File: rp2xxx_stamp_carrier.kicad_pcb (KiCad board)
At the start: 4 copper layers, 101.6 x 53.3 mm, 259 parts, among them J1 Conn_Stemma_QT, J10 Conn_01x10, J11 microSD, J12 Conn_01x08, J13 Conn_SPI, J14 Conn_01x08, J15 Conn_01x08, J16 Conn_01x08, J17 USB_C_Receptacle_USB2.0, J18 USB_A, J2 Conn_Pi_SWD, J3 Conn_Pi_UART, J4 Conn_Batt, J5 Barrel_Jack, J6 DVI-D_Mini, J8 Conn_PMOD, J9 Conn_01x08, Q1 DMG3415U-7, SW1 BTN_RESET, SW2 BTN_BOOTSEL, SW3 SW_USB, SW4 BTN_USR1, SW5 BTN_USR2, U1 XL1509-5.0, U2 MSUSB30, U3 RP2350_Stamp_XL

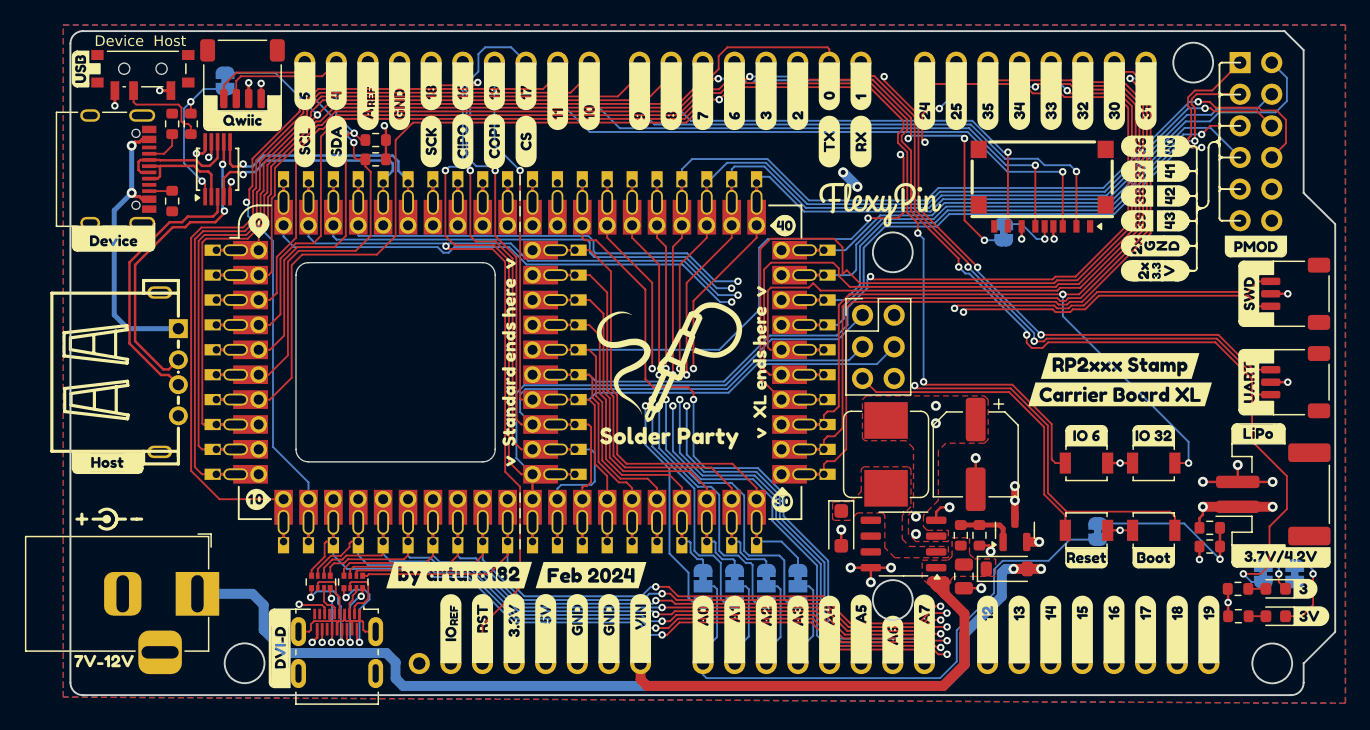
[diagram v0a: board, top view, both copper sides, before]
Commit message: Rev 2
Fixed HDMI connector
Swapped RST and BOOTSEL buttons to match Stamp
Added BAT_STAT to Stamp
Changed 2x silk back to single line
Adjusted Name silkscreen
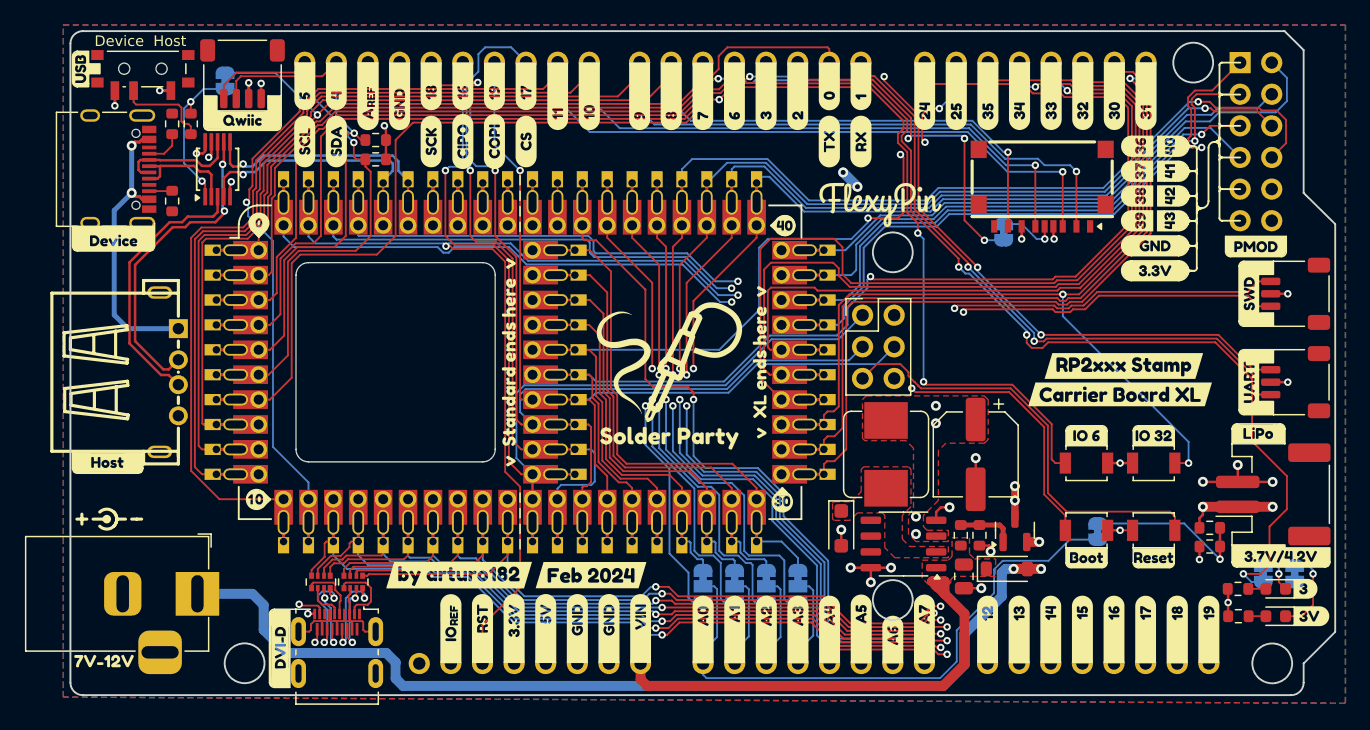
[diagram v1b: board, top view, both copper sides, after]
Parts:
- removed kibuzzard-65DBD93A (x2): G***, kibuzzard-65DBD93A
- removed kibuzzard-65DBD94E (x2): G***, kibuzzard-65DBD94E
- removed kibuzzard-65DBD952 (x2): G***, kibuzzard-65DBD952
- removed kibuzzard-65DBDA2E (x4): G***, kibuzzard-65DBDA2E
- removed kibuzzard-65DBDB16 (x2): G***, kibuzzard-65DBDB16
- removed kibuzzard-65DBDB2C (x2): G***, kibuzzard-65DBDB2C
- added kibuzzard-66063958: G***, kibuzzard-66063958, B.Cu at (195.4, 87.8)
- added kibuzzard-66063979: G***, kibuzzard-66063979, B.Cu at (195.4, 89.8)
- added kibuzzard-660639E8: G***, kibuzzard-660639E8, F.Cu at (195.7, 89.8)
- added kibuzzard-660639F3: G***, kibuzzard-660639F3, F.Cu at (195.7, 87.8)
- U3: value RP2350_Stamp_XL -> rp2xxx_Stamp_XL; footprint rp2350_stamp_carrier:RP2xx_Stamp_FlexyPin -> rp2xxx_stamp_carrier:RP2xx_Stamp_FlexyPin
- moved SW1 5.40 mm to (195.6, 110.6), turned to 0 degrees
- moved SW2 5.40 mm to (190.2, 110.6), turned to 180 degrees
- moved kibuzzard-65DBAE3B 5.40 mm to (195.6, 112.8)
- moved kibuzzard-65DBAE3E 5.40 mm to (190.2, 112.8)
- moved kibuzzard-65DBBE17 1.10 mm to (179.4, 101.3)
- moved kibuzzard-65DBBE25 0.80 mm to (181.7, 101.0)
- moved kibuzzard-65DBBE65 0.75 mm to (184.0, 100.6)
- moved kibuzzard-65DBBF1E 0.72 mm to (186.4, 100.2)
- moved kibuzzard-65DBBE17 0.30 mm to (193.2, 97.4)
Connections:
- J6 pad 1: GND -> unconnected-(J6-HPD/HEAC--Pad1)
- J6 pad 11: Net-(J6-CK+) -> Net-(J6-D0-)
- J6 pad 12: Net-(J6-CK-) -> Net-(J6-CK+)
- J6 pad 14: unconnected-(J6-CEC-Pad14) -> Net-(J6-CK-)
- J6 pad 15: /GPIO5 -> unconnected-(J6-CEC-Pad15)
- J6 pad 16: /GPIO4 -> GND
- J6 pad 17: unconnected-(J6-UTILITY/HEAC+-Pad17) -> /GPIO5
- J6 pad 18: +5V -> /GPIO4
- J6 pad 19: unconnected-(J6-HPD/HEAC--Pad19) -> +5V
- J6 pad 2: Net-(J6-D2+) -> unconnected-(J6-UTILITY/HEAC+-Pad2)
- J6 pad 3: Net-(J6-D2-) -> Net-(J6-D2+)
- J6 pad 5: Net-(J6-D1+) -> Net-(J6-D2-)
- J6 pad 6: Net-(J6-D1-) -> Net-(J6-D1+)
- J6 pad 8: Net-(J6-D0+) -> Net-(J6-D1-)
- J6 pad 9: Net-(J6-D0-) -> Net-(J6-D0+)
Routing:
- net /~{RESET}: track 120.8 -> 130.7 mm
- net /BOOTSEL: track 89.7 -> 81.2 mm
- net Net-(J6-D1+): track 2.35 -> 6.08 mm, vias 0 -> 2
- net Net-(J6-D0+): track 8.29 -> 4.91 mm, vias 2 -> 0
- net Net-(J6-CK+): track 2.70 -> 5.77 mm, vias 0 -> 2
- net Net-(J6-D2-): track 5.07 -> 2.16 mm
- net Net-(J6-D2+): track 8.47 -> 5.89 mm, vias 2 -> 0
- net Net-(J6-CK-): track 5.55 -> 8.06 mm
- net +5V: track 149.1 -> 151.1 mm
- net Net-(J6-D1-): track 6.05 -> 7.72 mm
- net unconnected-(U3A-BAT_STAT-Pad59): track 0.00 -> 1.55 mm
- net Net-(J6-D0-): track 4.45 -> 3.09 mm
- net GND: track 46.6 -> 45.9 mm

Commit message: Rev 3
- USB Switch jumper open by default
- Power USB Host from 5V not VBUS
- Fix SPI pin silkscreen
- Add test points for USB D+/D-
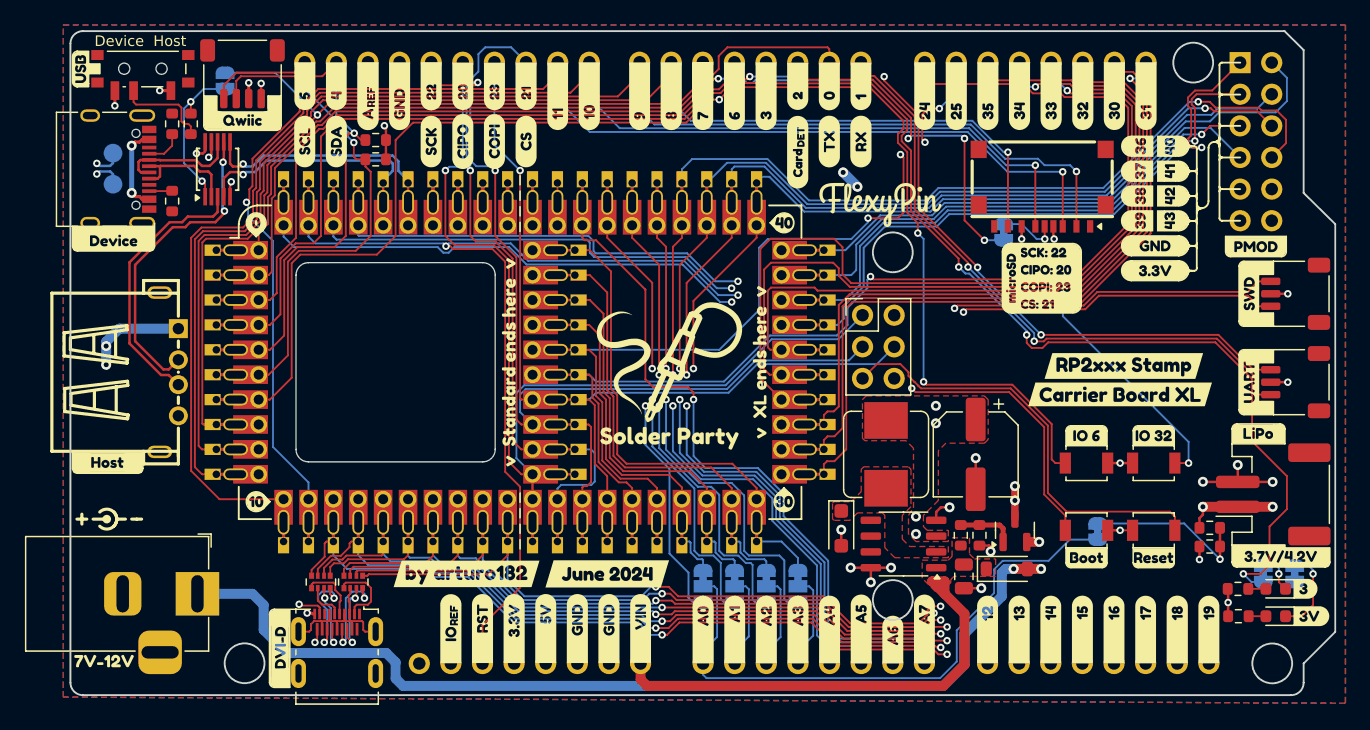
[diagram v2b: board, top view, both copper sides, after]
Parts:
- removed ? (x2): , buzzardLabel
- removed kibuzzard-653BCEA0: G***, kibuzzard-653BCEA0
- removed kibuzzard-653BD19C: G***, kibuzzard-653BD19C
- removed kibuzzard-65DA1421: G***, kibuzzard-65DA1421
- removed kibuzzard-65DA43F2: G***, kibuzzard-65DA43F2
- removed kibuzzard-65DA43F6: G***, kibuzzard-65DA43F6
- removed kibuzzard-65DA43F9: G***, kibuzzard-65DA43F9
- removed kibuzzard-65DA43FD: G***, kibuzzard-65DA43FD
- removed kibuzzard-65DB92FF: G***, kibuzzard-65DB92FF
- removed kibuzzard-65DB9306: G***, kibuzzard-65DB9306
- removed kibuzzard-65DB930D: G***, kibuzzard-65DB930D
- removed kibuzzard-65DB9314: G***, kibuzzard-65DB9314
- removed kibuzzard-65DBBF1E (x2): G***, kibuzzard-65DBBF1E
- added TP1: TP_USB_D+, TestPoint:TestPoint_Pad_D1.5mm, B.Cu at (112.0, 82.8)
- added TP2: TP_USB_D-, TestPoint:TestPoint_Pad_D1.5mm, B.Cu at (112.0, 80.3)
- added kibuzzard-65DA4391: G***, kibuzzard-65DA4391, F.Cu at (167.0, 77.8)
- added kibuzzard-65DA4391: G***, kibuzzard-65DA4391, F.Cu at (167.0, 82.7)
- added kibuzzard-668C75B1: G***, kibuzzard-668C75B1, F.Cu at (137.6, 74.9)
- added kibuzzard-668C75C6: G***, kibuzzard-668C75C6, F.Cu at (140.1, 74.9)
- added kibuzzard-668C75DA: G***, kibuzzard-668C75DA, F.Cu at (142.6, 74.9)
- added kibuzzard-668C7671: G***, kibuzzard-668C7671, F.Cu at (145.2, 74.9)
- added kibuzzard-668C76A7: G***, kibuzzard-668C76A7, B.Cu at (145.2, 75.0)
- added kibuzzard-668C7736: G***, kibuzzard-668C7736, B.Cu at (142.6, 75.0)
- added kibuzzard-668C7740: G***, kibuzzard-668C7740, B.Cu at (140.1, 75.0)
- added kibuzzard-668C7764: G***, kibuzzard-668C7764, B.Cu at (137.6, 74.9)
- added kibuzzard-668C8744: G***, kibuzzard-668C8744, F.Cu at (167.0, 74.9)
- added kibuzzard-668C88D6: G***, kibuzzard-668C88D6, F.Cu at (167.2, 79.0)
- added kibuzzard-668C88F2: G***, kibuzzard-668C88F2, F.Cu at (167.0, 81.1)
- added kibuzzard-668C89D9: G***, kibuzzard-668C89D9, F.Cu at (159.4, 74.9)
- added kibuzzard-668C9122: G***, kibuzzard-668C9122, F.Cu at (184.1, 90.3)
- added kibuzzard-668C9182: G***, kibuzzard-668C9182, F.Cu at (186.9, 90.3)
- added kibuzzard-668C9635: G***, kibuzzard-668C9635, B.Cu at (112.0, 78.2)
- added kibuzzard-668C97F2: G***, kibuzzard-668C97F2, B.Cu at (112.0, 84.9)
- added kibuzzard-6695ACF2: G***, kibuzzard-6695ACF2, F.Cu at (123.5, 108.3)
- added kibuzzard-6695AD18: G***, kibuzzard-6695AD18, F.Cu at (123.5, 85.9)
- added kibuzzard-6695BF60: G***, kibuzzard-6695BF60, F.Cu at (165.9, 108.3)
- added kibuzzard-6695BFEA: G***, kibuzzard-6695BFEA, F.Cu at (165.9, 85.9)
- added kibuzzard-6695CF81: G***, kibuzzard-6695CF81, F.Cu at (151.7, 114.1)
- added kibuzzard-6695CF95: G***, kibuzzard-6695CF95, B.Cu at (186.4, 100.2)
- J6: value DVI-D_Mini -> DVI-D_Micro
- JP4: footprint Jumper:SolderJumper-2_P1.3mm_Bridged_RoundedPad1.0x1.5mm -> Jumper:SolderJumper-2_P1.3mm_Open_RoundedPad1.0x1.5mm
- moved kibuzzard-65DBBE65 0.61 mm to (140.4, 114.1)
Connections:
- J18 pad 1: VBUS -> +5V
- U3 pad 59: unconnected-(U3A-BAT_STAT-Pad59) -> /BAT_STAT
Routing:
- net +5V: track 151.1 -> 188.4 mm, vias 8 -> 10
- net /USB_D+: track 19.1 -> 33.6 mm, vias 1 -> 2
- net /USB_D-: track 19.5 -> 33.9 mm, vias 1 -> 2
- net VBUS: track 118.7 -> 113.0 mm
- net unconnected-(U3A-BAT_STAT-Pad59): track 1.55 -> 0.00 mm
- net /BAT_STAT: track 0.00 -> 1.55 mm

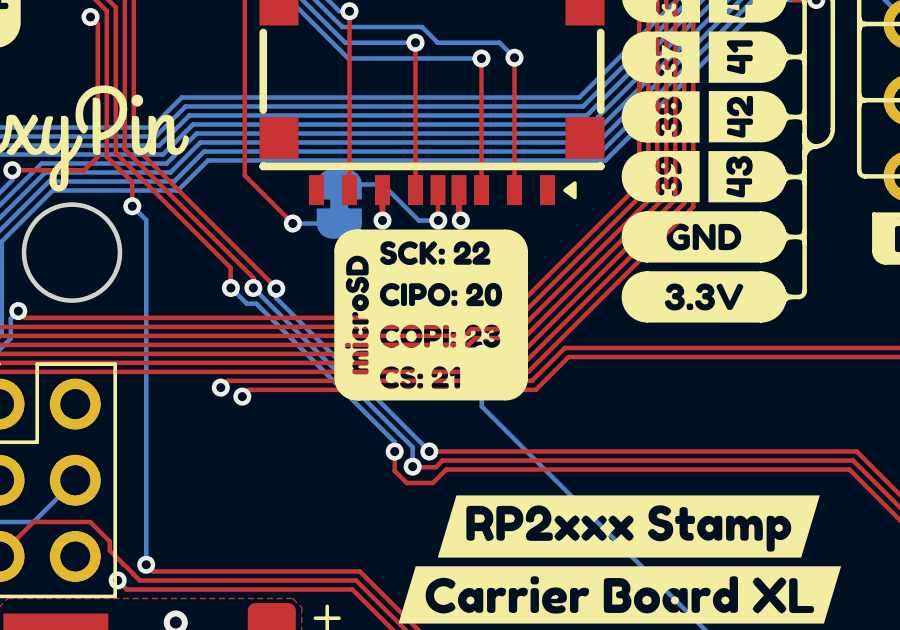
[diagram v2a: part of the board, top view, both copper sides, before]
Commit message: Rev 3.1, add README, and LICENSE
- Fixed the microSD pin silkscreen
- Updated BOM
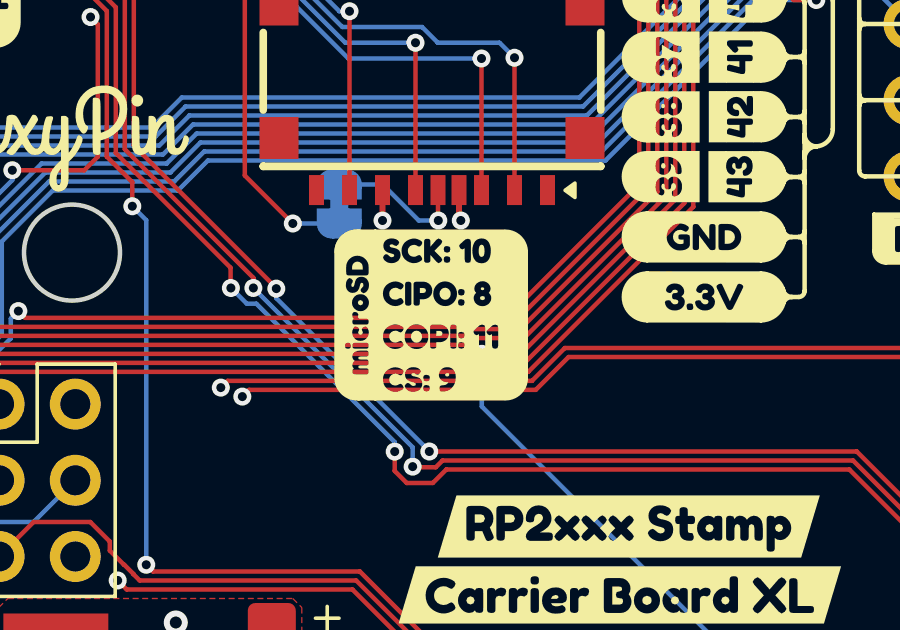
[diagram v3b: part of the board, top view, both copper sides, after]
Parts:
- removed kibuzzard-668C9182: G***, kibuzzard-668C9182
- added kibuzzard-669714D3: G***, kibuzzard-669714D3, F.Cu at (186.9, 90.3)
- J1: value Conn_Stemma_QT -> Conn_Qwiic
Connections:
- U3 pad 59: /BAT_STAT -> unconnected-(U3A-BAT_STAT-Pad59)_0
- U3 pad 60: /LDO_EN -> unconnected-(U3A-LDO_EN-Pad60)_2
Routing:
- net (no net): track 0.00 -> 3.10 mm
- net /LDO_EN: track 1.55 -> 0.00 mm
- net /BAT_STAT: track 1.55 -> 0.00 mm
